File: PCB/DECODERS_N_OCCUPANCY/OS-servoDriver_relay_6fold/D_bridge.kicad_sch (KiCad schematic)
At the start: 5 parts

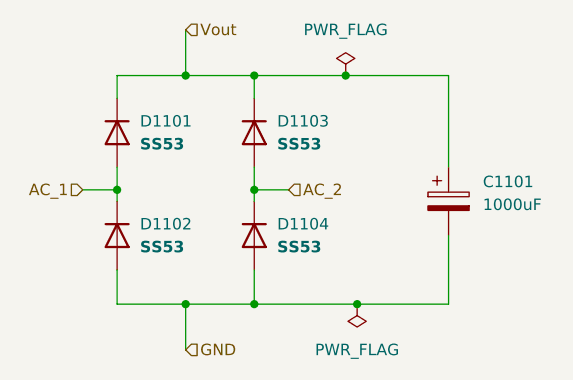
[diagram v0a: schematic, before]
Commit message: Added public licences to all of train-science DIY code. I do need to strip this from NMRA library though
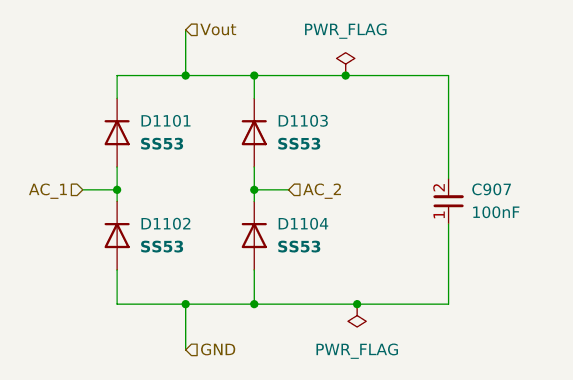
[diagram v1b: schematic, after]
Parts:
- removed C1101: 1000uF, Capacitor_SMD:CP_Elec_8x10.5, symbol Device:C_Polarized
- added C907: 100nF, Capacitor_SMD:C_0805_2012Metric_Pad1.18x1.45mm_HandSolder, symbol capacitor_miscellaneous:C_0805_100nF
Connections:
- net GND: now also C907.1
- net Vout: now also C907.2
